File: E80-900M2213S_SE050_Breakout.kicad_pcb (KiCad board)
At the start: 2 copper layers, 68.9 x 51.8 mm, 18 parts, among them IC2 SE050E2HQ1_Z01Z3Z, J1 Conn_01x12_Pin, U1 E80-900M2213S

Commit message: Fix R6 to 10k and name the radio interrupt DIO9
R6, the pull-up on the module's NRESET line, was entered as 4.7k; the
intended value is 10k.

Header pin 7 carries the LR1121's interrupt, which the module brings out as
DIO9 on pin 22. The net and the silkscreen called it DIO1, the SX126x name,
so anyone wiring it by label would have looked for the wrong signal. The net
is now LDI09 and the legend reads DIO9. The copper is unchanged: the
regenerated copper gerbers draw the same geometry and differ only in the net
attribute.

Regenerate gerber/ and the zip, refresh both board images, and bring the
README's pinout and bill of materials in line.

Co-Authored-By: Claude Opus 5.5 <noreply@anthropic.com>
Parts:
- R6: value 4.7K -> 10K
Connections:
- net LDI01 renamed LDI09
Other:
- board text added: "DIO9"
- board text removed: "DIO1"
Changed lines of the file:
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@@
 			(layers "*.Cu" "*.Mask")
 			(remove_unused_layers no)
-			(net "LDI01")
+			(net "LDI09")
 			(pinfunction "Pin_7_7")
 			(pintype "passive")
@@
 			(size 1.5 0.8)
 			(layers "F.Cu" "F.Mask" "F.Paste")
-			(net "LDI01")
+			(net "LDI09")
 			(pinfunction "DIO9_22")
 			(pintype "output")
@@
 			)
 		)
-		(property "Value" "4.7K"
+		(property "Value" "10K"
 			(at 0 1.43 0)
 			(layer "F.Fab")
@@
 		)
 	)
-	(gr_text "DIO1"
+	(gr_text "DIO9"
 		(at 113.3 61.52 0)
 		(layer "F.SilkS")
@@
 	)
 	(segment
-		(start 142.63 58.15)
-		(end 140.53 58.15)
-		(width 0.6)
-		(layer "F.Cu")
-		(net "LDI01")
-	)
-	(via
-		(at 142.63 58.15)
-		(size 0.6)
-		(drill 0.3)
-		(layers "F.Cu" "B.Cu")
-		(net "LDI01")
-	)
-	(segment
-		(start 111.51 61.32)
-		(end 111.1 60.91)
-		(width 0.3)
-		(layer "B.Cu")
-		(net "LDI01")
-	)
-	(segment
-		(start 135.1 61.32)
-		(end 111.51 61.32)
-		(width 0.3)
-		(layer "B.Cu")
-		(net "LDI01")
-	)
-	(segment
-		(start 142.63 58.15)
-		(end 138.27 58.15)
-		(width 0.3)
-		(layer "B.Cu")
-		(net "LDI01")
-	)
-	(segment
-		(start 138.27 58.15)
-		(end 135.1 61.32)
-		(width 0.3)
-		(layer "B.Cu")
-		(net "LDI01")
-	)
-	(segment
 		(start 142.63 59.42)
 		(end 140.53 59.42)
@@
 		(net "Net-(IC2-VCC)")
 	)
+	(segment
+		(start 142.63 58.15)
+		(end 140.53 58.15)
+		(width 0.6)
+		(layer "F.Cu")
+		(net "LDI09")
+	)
+	(via
+		(at 142.63 58.15)
+		(size 0.6)
+		(drill 0.3)
+		(layers "F.Cu" "B.Cu")
+		(net "LDI09")
+	)
+	(segment
+		(start 111.51 61.32)
+		(end 111.1 60.91)
+		(width 0.3)
+		(layer "B.Cu")
+		(net "LDI09")
+	)
+	(segment
+		(start 135.1 61.32)
+		(end 111.51 61.32)
+		(width 0.3)
+		(layer "B.Cu")
+		(net "LDI09")
+	)
+	(segment
+		(start 142.63 58.15)
+		(end 138.27 58.15)
+		(width 0.3)
+		(layer "B.Cu")
+		(net "LDI09")
+	)
+	(segment
+		(start 138.27 58.15)
+		(end 135.1 61.32)
+		(width 0.3)
+		(layer "B.Cu")
+		(net "LDI09")
+	)
 	(zone

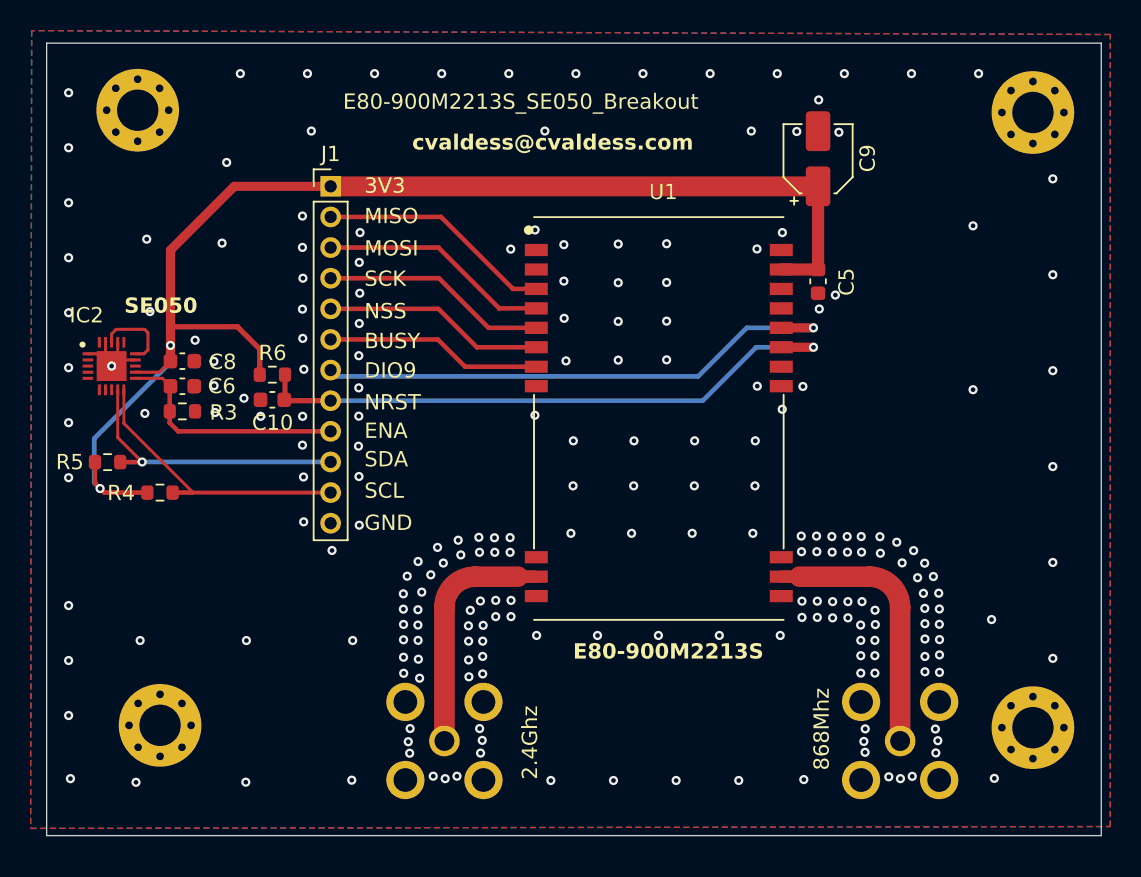
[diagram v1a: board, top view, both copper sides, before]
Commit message: Widen the host header to 14 pins and ground the SE050 pad through five vias
The host connector is now a 1x14 2.54 mm header (J2) instead of the
1x12 2.00 mm one. The two extra pins bring out the LR1121's DIO7 and DIO8
(module pins 24 and 23), which were left unconnected before. The other
signals keep their order and move down two positions: DIO9 is now pin 9,
NRST 10, ENA 11, SDA 12, SCL 13 and GND 14.

The SE050's exposed pad had a single via to the ground plane, in its
centre. Four more 0.3 mm vias go under the four paste windows, which is
the five-via pattern of the se050-breakout board that was validated on
hardware.

Regenerate gerber/ and the zip (297 plated holes: 237 vias and 60 pads),
refresh both board images, and update the README's pinout, bill of
materials and hole count.

Co-Authored-By: Claude Opus 5.5 <noreply@anthropic.com>
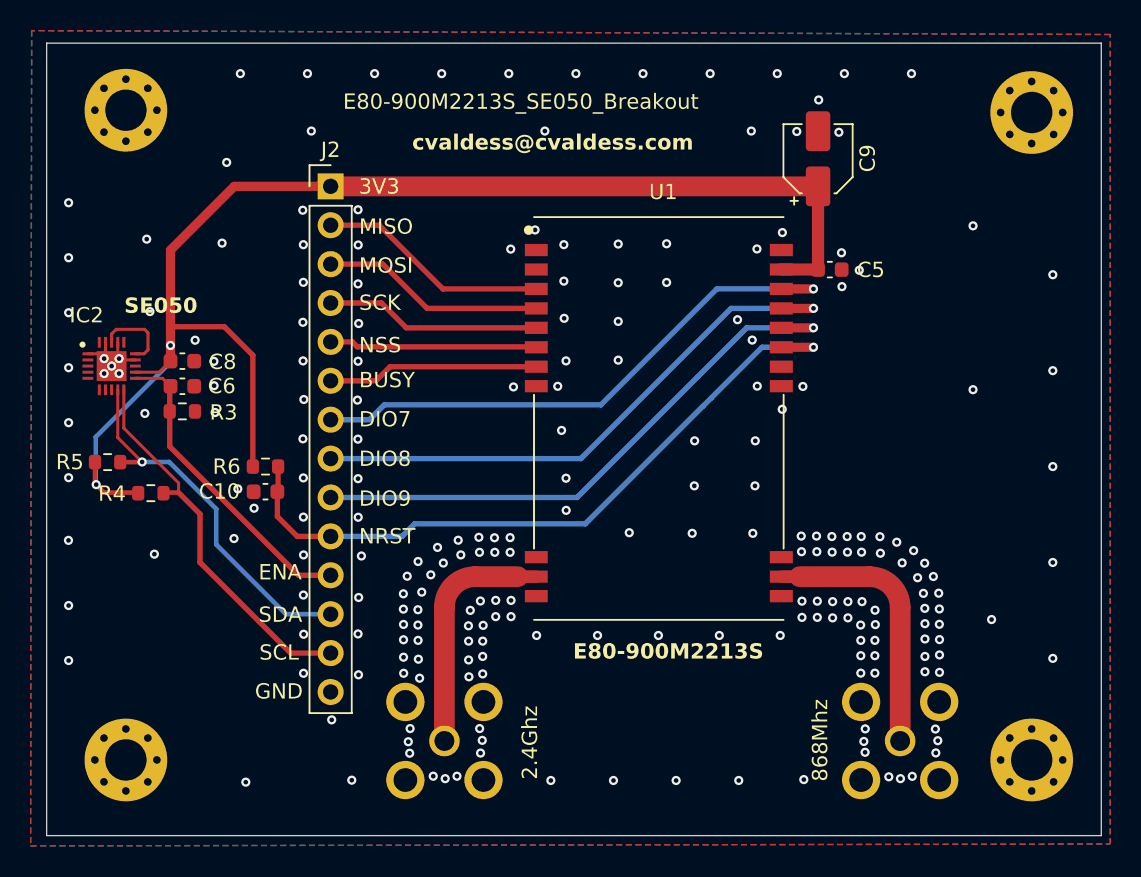
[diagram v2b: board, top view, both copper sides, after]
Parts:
- removed J1: Conn_01x12_Pin, Connector_PinHeader_2.00mm:PinHeader_1x12_P2.00mm_Vertical
- added J2: Conn_01x14_Pin, Connector_PinHeader_2.54mm:PinHeader_1x14_P2.54mm_Vertical, F.Cu at (111.1, 48.9)
- moved C10 6.02 mm to (106.8, 68.8)
- moved R6 6.02 mm to (106.8, 67.2)
- moved H3 3.18 mm to (97.7, 86.4)
- moved H4 2.11 mm to (156.9, 86.4)
- moved C5 1.09 mm to (143.7, 54.4), turned to 0 degrees
- moved H1 0.77 mm to (97.7, 43.9)
- moved R4 0.60 mm to (99.4, 69.0)
- moved H2 0.08 mm to (156.9, 44.1)
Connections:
- U1 pad 23: unconnected-(U1-DIO8-Pad23) -> LDIO8
- U1 pad 24: unconnected-(U1-DIO7-Pad24) -> LDIO7
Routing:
- net LDIO8: track 0.00 -> 37.7 mm, vias 0 -> 1
- net LDIO7: track 0.00 -> 37.2 mm, vias 0 -> 1
- net SCL: track 18.9 -> 25.3 mm
- net LNRST: track 39.8 -> 46.0 mm
- net SDA: track 19.1 -> 24.6 mm
- net SE_ENA: track 15.7 -> 20.5 mm
- net +3.3V: track 86.2 -> 90.5 mm
- net LDI09: track 35.1 -> 38.2 mm
- net LNSS: track 14.5 -> 13.6 mm
- net LSCK: track 14.8 -> 14.1 mm
- net GND: vias 228 -> 230
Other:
- board text added: "DIO7"
- board text added: "DIO8"
